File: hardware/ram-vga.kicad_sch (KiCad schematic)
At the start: 34 parts, among them J11 Conn_01x04_Male, J6 DB15_Female_HighDensity, J7 Conn_01x12_Male, U10 74HC245, U11 74HC245, U12 74HC109, U14 74HC04, U16 62256, U17 74HC00, U18 w27C512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

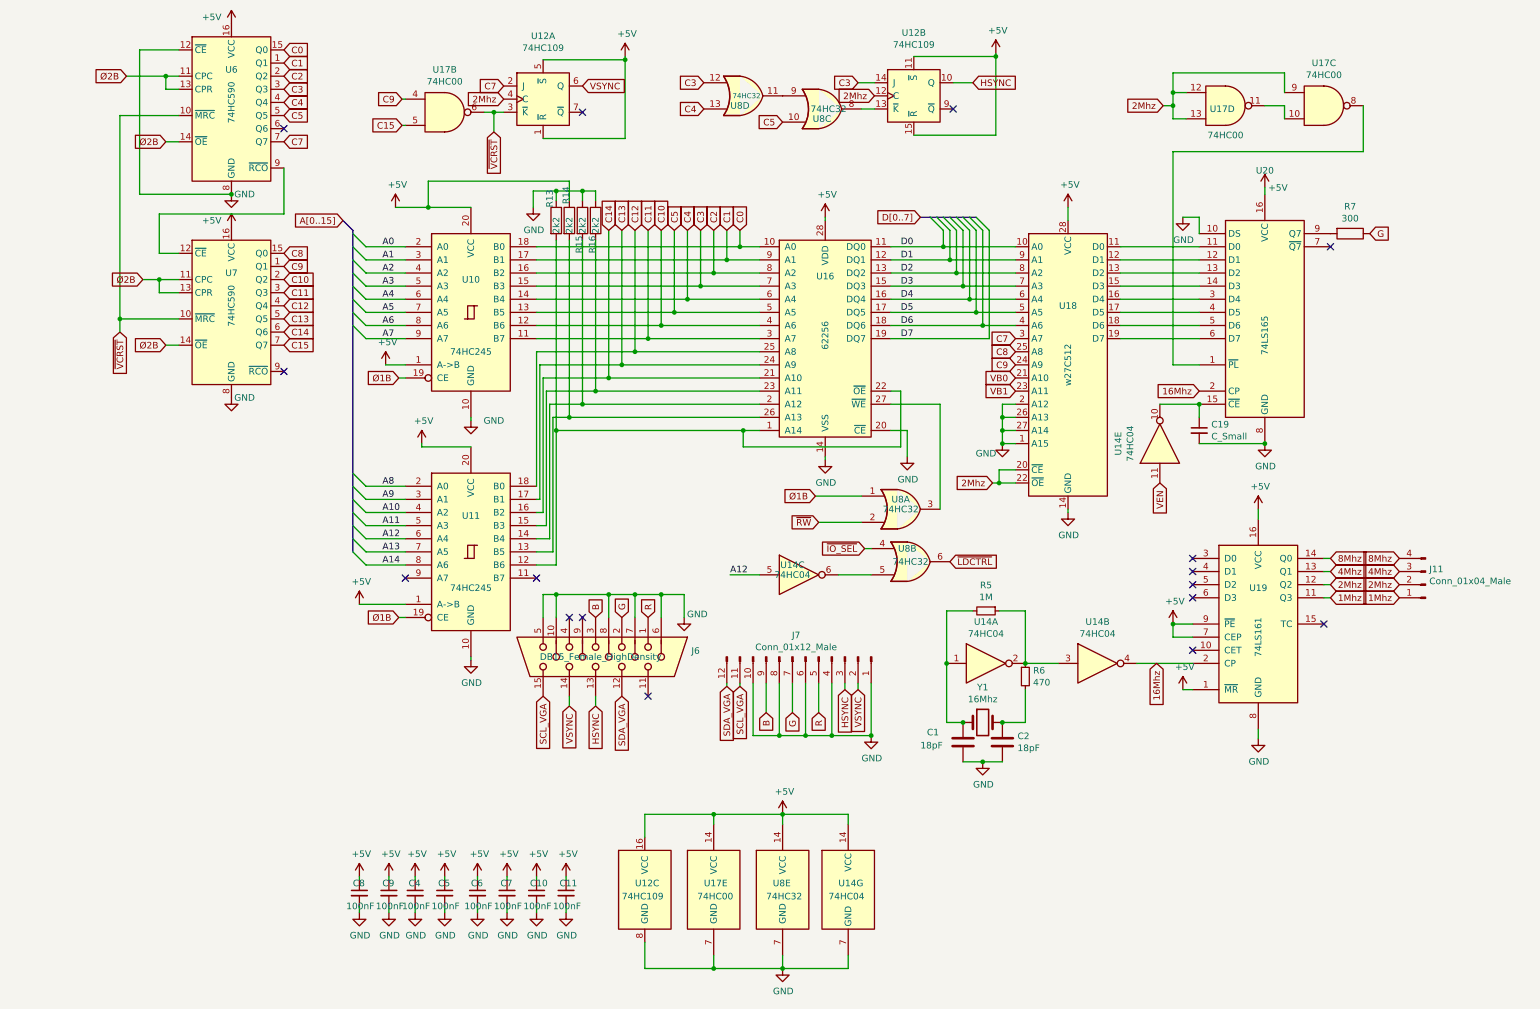
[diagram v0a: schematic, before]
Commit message: PS/2 via shift register upgrade!
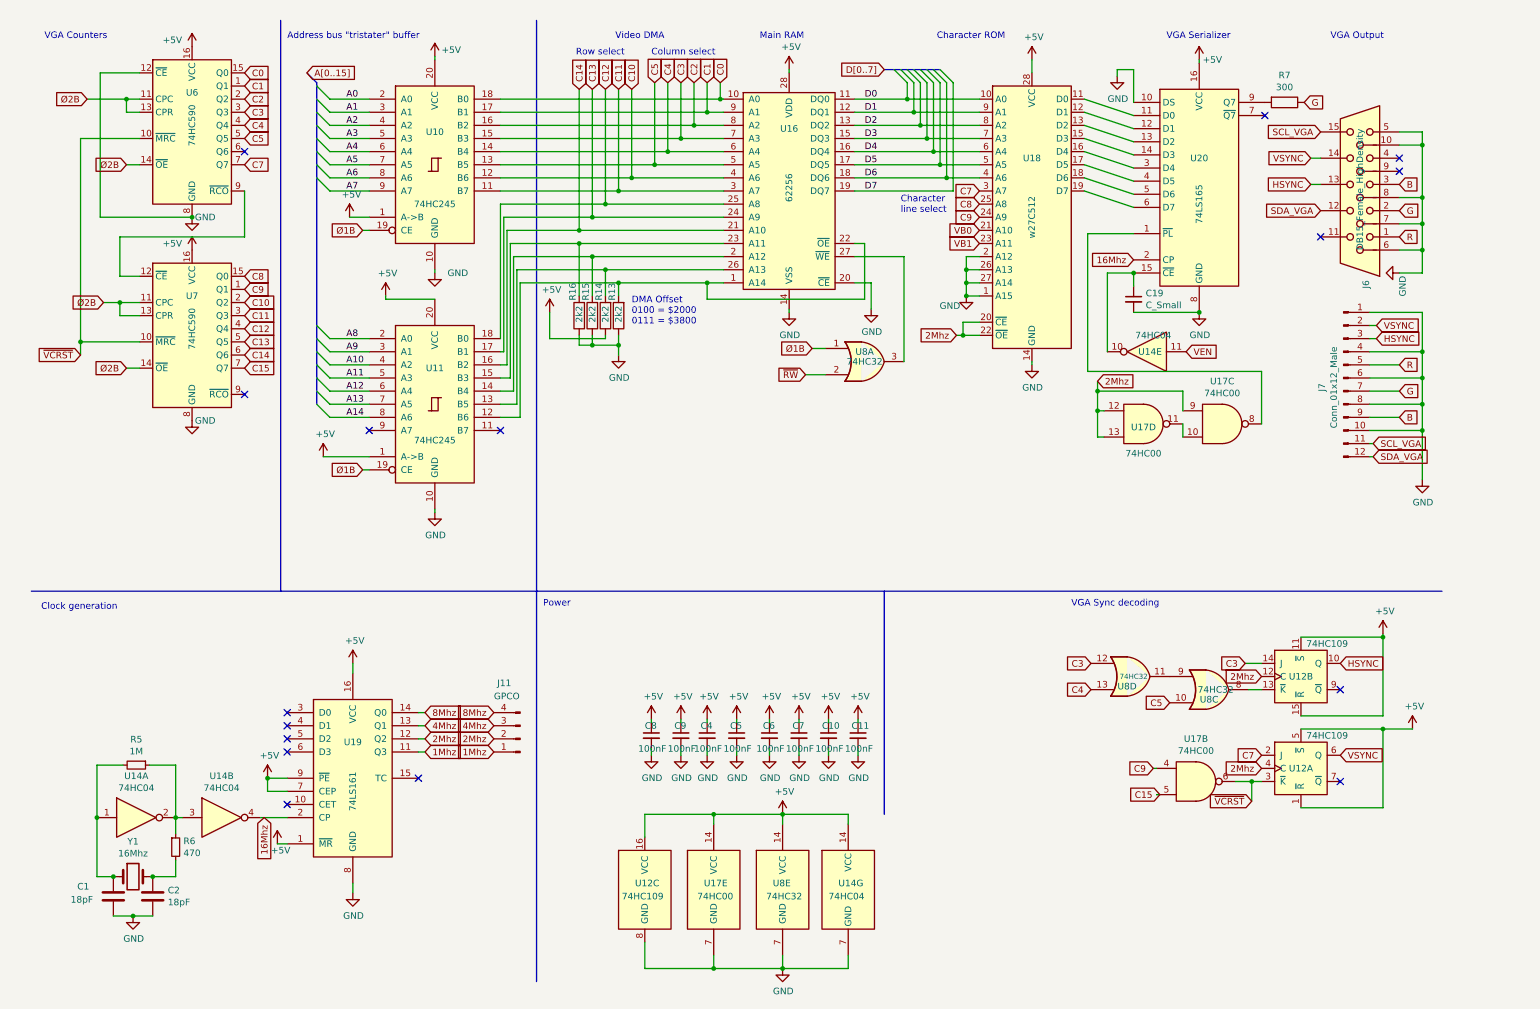
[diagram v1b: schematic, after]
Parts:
- removed unit 3 of U14
- removed unit 2 of U8
- J11: value Conn_01x04_Male -> GPCO
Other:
- note added: "Address bus "tristater" buffer"
- note added: "Character ROM"
- note added: "Character line select"
- note added: "Clock generation"
- note added: "Column select"
- note added: "DMA Offset 0100 = $2000 0111 = $3800"
- note added: "Main RAM"
- note added: "Power"
- note added: "Row select"
- note added: "VGA Counters"
- note added: "VGA Output"
- note added: "VGA Serializer"
- note added: "VGA Sync decoding"
- note added: "Video DMA"
- moved on the sheet: C1, C10, C11, C19, C2, C4, C5, C6, C7, C8, C9, J11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

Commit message: R1B2 gerbers, start+stop bits in modem driver
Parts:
- added R17, R19, R20, R21, R23, R24, R25: NC, Resistor_SMD:R_0805_2012Metric, symbol Device:R
- added R18, R22: 2k2, Resistor_SMD:R_0805_2012Metric, symbol Device:R
- added R26: 0R, Resistor_SMD:R_0402_1005Metric, symbol Device:R
- added R27: NC, Resistor_SMD:R_0402_1005Metric, symbol Device:R
- added R30: NC, Resistor_SMD:R_0402_1005Metric_Pad0.72x0.64mm_HandSolder, symbol Device:R_Small
- added R31, R32, R33, R34, R35, R36, R37, R38, R39, R40, R41, R42, R43, R44, R45, R46: NC, Resistor_SMD:R_0402_1005Metric, symbol Device:R_Small
- added unit 3 of U14
- added U21: 74HC00, Package_DIP:DIP-14_W7.62mm, symbol 74xx:74HC00
- C1, C2: symbol Device:C -> Device:C_Small
- J11: footprint Connector_PinHeader_2.54mm:PinHeader_1x04_P2.54mm_Vertical -> Connector_PinHeader_2.54mm:PinHeader_1x05_P2.54mm_Vertical; symbol Connector:Conn_01x04_Male -> Connector:Conn_01x05_Male
- R16: value 2k2 -> NC
- R7: value 300 -> 150
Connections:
- net +5V: now also R18.1, R19.1, R20.1, R21.1, R30.1; no longer R14.1
- net 16Mhz: now also J11.5 (Pin_5)
- net A0: now also R31.1
- net A1: now also R32.1
- net A10: now also R41.1
- net A11: now also R42.1
- net A12: now also R43.1
- net A13: now also R44.1
- net A14: now also R45.1
- net A2: now also R33.1
- net A3: now also R34.1
- net A4: now also R35.1
- net A5: now also R36.1
- net A6: now also R37.1
- net A7: now also R38.1
- net A8: now also R39.1
- net A9: now also R40.1
- net C0: now also R31.2
- net C1: now also R32.2
- net C10: now also R37.2
- net C11: now also R38.2
- net C12: now also R39.2
- net C13: now also R40.2
- net C14: now also R41.2
- net C2: now also R33.2
- net C3: now also R34.2
- net C4: now also R35.2
- net C5: now also R36.2
- net C7: now also U18.25 (A8); no longer U18.3 (A7)
- net C8: now also U18.24 (A9); no longer U18.25 (A8)
- net C9: now also U18.21 (A10); no longer U18.24 (A9)
- net D7: now also U18.3 (A7)
- net GND: now also R14.1, R22.1; no longer U16.20 (~{CE}), U18.2 (A12)
- net VB0: now also U18.23 (A11); no longer U18.21 (A10)
- net VB1: now also U18.2 (A12); no longer U18.23 (A11)
- net Ø1B: now also U17.10, U17.11
- net at R13.2, U11.12 (B6), U16.1 (A14): now also R21.2, R23.2, R27.2, R45.2, U21.9; no longer U16.22 (~{OE})
- net at R15.2, U11.14 (B4), U16.2 (A12): now also R19.2, R25.2, R43.2
- net at R16.2, U11.15 (B3), U16.23 (A11): now also R17.2, R18.2, R42.2
- net at R14.2, U11.13 (B5), U16.26 (A13): now also R20.2, R24.2, R26.2, R44.2
- net at U11.11 (B7): now also U16.20 (~{CE}), R22.2, R46.2
- net A15: now reaches U11.9 (A7)
- net A15: now also R46.1
- net at J6.9: now also R30.2
- new net: U14.6, U16.22 (~{OE})
- new net: R26.1, R27.1, U21.10
- new net: U14.5, U21.8
- new net CTRL3: R17.1
- new net CTRL4: R25.1
- new net CTRL5: R24.1
- new net CTRL6: R23.1
- no-connect marks 16 -> 13
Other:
- note added: "DMA Offset A14 - A11 0001 = $0800 0100 = $2000 0111 = $3800 1000 = $4000 1011 = $5800 1100 = $6000 (Not allowed)"
- note removed: "DMA Offset 0100 = $2000 0111 = $3800"
- moved on the sheet: R13, R14, R15, R16

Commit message: Solder jumpers instead of 0402 resistors, redundant 0805 decoupling caps
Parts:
- R26, R27, R31, R32, R33, R34, R35, R36, R37, R38, R39, R40, R41, R42, R43, R44, R45, R46: footprint Resistor_SMD:R_0402_1005Metric -> Jumper:SolderJumper-2_P1.3mm_Open_RoundedPad1.0x1.5mm
- R30: footprint Resistor_SMD:R_0402_1005Metric_Pad0.72x0.64mm_HandSolder -> Jumper:SolderJumper-2_P1.3mm_Open_RoundedPad1.0x1.5mm
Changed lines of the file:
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@@
       (effects (font (size 0.8 0.8)))
     )
-    (property "Footprint" "Resistor_SMD:R_0402_1005Metric" (id 2) (at 88.265 86.36 0)
+    (property "Footprint" "Jumper:SolderJumper-2_P1.3mm_Open_RoundedPad1.0x1.5mm" (id 2) (at 88.265 86.36 0)
       (effects (font (size 1.27 1.27)) hide)
     )
@@
       (effects (font (size 0.8 0.8)))
     )
-    (property "Footprint" "Resistor_SMD:R_0402_1005Metric" (id 2) (at 88.265 81.28 0)
+    (property "Footprint" "Jumper:SolderJumper-2_P1.3mm_Open_RoundedPad1.0x1.5mm" (id 2) (at 88.265 81.28 0)
       (effects (font (size 1.27 1.27)) hide)
     )
@@
       (effects (font (size 0.8 0.8)))
     )
-    (property "Footprint" "Resistor_SMD:R_0402_1005Metric" (id 2) (at 88.265 78.74 0)
+    (property "Footprint" "Jumper:SolderJumper-2_P1.3mm_Open_RoundedPad1.0x1.5mm" (id 2) (at 88.265 78.74 0)
       (effects (font (size 1.27 1.27)) hide)
     )
@@
       (effects (font (size 0.8 0.8)))
     )
-    (property "Footprint" "Resistor_SMD:R_0402_1005Metric" (id 2) (at 88.265 91.44 0)
+    (property "Footprint" "Jumper:SolderJumper-2_P1.3mm_Open_RoundedPad1.0x1.5mm" (id 2) (at 88.265 91.44 0)
       (effects (font (size 1.27 1.27)) hide)
     )
@@
       (effects (font (size 0.8 0.8)))
     )
-    (property "Footprint" "Resistor_SMD:R_0402_1005Metric" (id 2) (at 88.265 83.82 0)
+    (property "Footprint" "Jumper:SolderJumper-2_P1.3mm_Open_RoundedPad1.0x1.5mm" (id 2) (at 88.265 83.82 0)
       (effects (font (size 1.27 1.27)) hide)
     )
@@
       (effects (font (size 0.8 0.8)))
     )
-    (property "Footprint" "Resistor_SMD:R_0402_1005Metric" (id 2) (at 88.265 45.085 0)
+    (property "Footprint" "Jumper:SolderJumper-2_P1.3mm_Open_RoundedPad1.0x1.5mm" (id 2) (at 88.265 45.085 0)
       (effects (font (size 1.27 1.27)) hide)
     )
@@
       (effects (font (size 0.8 0.8)))
     )
-    (property "Footprint" "Resistor_SMD:R_0402_1005Metric" (id 2) (at 88.265 88.9 0)
+    (property "Footprint" "Jumper:SolderJumper-2_P1.3mm_Open_RoundedPad1.0x1.5mm" (id 2) (at 88.265 88.9 0)
       (effects (font (size 1.27 1.27)) hide)
     )
@@
       (effects (font (size 0.8 0.8)))
     )
-    (property "Footprint" "Resistor_SMD:R_0402_1005Metric" (id 2) (at 88.265 73.66 0)
+    (property "Footprint" "Jumper:SolderJumper-2_P1.3mm_Open_RoundedPad1.0x1.5mm" (id 2) (at 88.265 73.66 0)
       (effects (font (size 1.27 1.27)) hide)
     )
@@
       (effects (font (size 1.27 1.27)) (justify left))
     )
-    (property "Footprint" "Resistor_SMD:R_0402_1005Metric_Pad0.72x0.64mm_HandSolder" (id 2) (at 283.21 38.735 0)
+    (property "Footprint" "Jumper:SolderJumper-2_P1.3mm_Open_RoundedPad1.0x1.5mm" (id 2) (at 283.21 38.735 0)
       (effects (font (size 1.27 1.27)) hide)
     )
@@
       (effects (font (size 1.27 1.27)) (justify left))
     )
-    (property "Footprint" "Resistor_SMD:R_0402_1005Metric" (id 2) (at 146.558 80.01 90)
+    (property "Footprint" "Jumper:SolderJumper-2_P1.3mm_Open_RoundedPad1.0x1.5mm" (id 2) (at 146.558 80.01 90)
       (effects (font (size 1.27 1.27)) hide)
     )
@@
       (effects (font (size 0.8 0.8)))
     )
-    (property "Footprint" "Resistor_SMD:R_0402_1005Metric" (id 2) (at 88.265 34.925 0)
+    (property "Footprint" "Jumper:SolderJumper-2_P1.3mm_Open_RoundedPad1.0x1.5mm" (id 2) (at 88.265 34.925 0)
       (effects (font (size 1.27 1.27)) hide)
     )
@@
       (effects (font (size 0.8 0.8)))
     )
-    (property "Footprint" "Resistor_SMD:R_0402_1005Metric" (id 2) (at 88.265 32.385 0)
+    (property "Footprint" "Jumper:SolderJumper-2_P1.3mm_Open_RoundedPad1.0x1.5mm" (id 2) (at 88.265 32.385 0)
       (effects (font (size 1.27 1.27)) hide)
     )
@@
       (effects (font (size 0.8 0.8)))
     )
-    (property "Footprint" "Resistor_SMD:R_0402_1005Metric" (id 2) (at 88.265 29.845 0)
+    (property "Footprint" "Jumper:SolderJumper-2_P1.3mm_Open_RoundedPad1.0x1.5mm" (id 2) (at 88.265 29.845 0)
       (effects (font (size 1.27 1.27)) hide)
     )
@@
       (effects (font (size 0.8 0.8)))
     )
-    (property "Footprint" "Resistor_SMD:R_0402_1005Metric" (id 2) (at 88.265 76.2 0)
+    (property "Footprint" "Jumper:SolderJumper-2_P1.3mm_Open_RoundedPad1.0x1.5mm" (id 2) (at 88.265 76.2 0)
       (effects (font (size 1.27 1.27)) hide)
     )
@@
       (effects (font (size 0.8 0.8)))
     )
-    (property "Footprint" "Resistor_SMD:R_0402_1005Metric" (id 2) (at 88.265 42.545 0)
+    (property "Footprint" "Jumper:SolderJumper-2_P1.3mm_Open_RoundedPad1.0x1.5mm" (id 2) (at 88.265 42.545 0)
       (effects (font (size 1.27 1.27)) hide)
     )
@@
       (effects (font (size 0.8 0.8)))
     )
-    (property "Footprint" "Resistor_SMD:R_0402_1005Metric" (id 2) (at 88.265 37.465 0)
+    (property "Footprint" "Jumper:SolderJumper-2_P1.3mm_Open_RoundedPad1.0x1.5mm" (id 2) (at 88.265 37.465 0)
       (effects (font (size 1.27 1.27)) hide)
     )
@@
       (effects (font (size 1.27 1.27)) (justify left))
     )
-    (property "Footprint" "Resistor_SMD:R_0402_1005Metric" (id 2) (at 149.733 80.01 90)
+    (property "Footprint" "Jumper:SolderJumper-2_P1.3mm_Open_RoundedPad1.0x1.5mm" (id 2) (at 149.733 80.01 90)
       (effects (font (size 1.27 1.27)) hide)
     )
@@
       (effects (font (size 0.8 0.8)))
     )
-    (property "Footprint" "Resistor_SMD:R_0402_1005Metric" (id 2) (at 88.265 40.005 0)
+    (property "Footprint" "Jumper:SolderJumper-2_P1.3mm_Open_RoundedPad1.0x1.5mm" (id 2) (at 88.265 40.005 0)
       (effects (font (size 1.27 1.27)) hide)
     )
@@
       (effects (font (size 0.8 0.8)))
     )
-    (property "Footprint" "Resistor_SMD:R_0402_1005Metric" (id 2) (at 88.265 27.305 0)
-      (effects (font (size 1.27 1.27)) hide)
-    )
+    (property "Footprint" "Jumper:SolderJumper-2_P1.3mm_Open_RoundedPad1.0x1.5mm" (id 2) (at 88.265 27.305 0)
+      (effects (font (size 1.27 1.27)) hide)
+    )
